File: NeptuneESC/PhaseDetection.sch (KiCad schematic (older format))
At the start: 9 parts

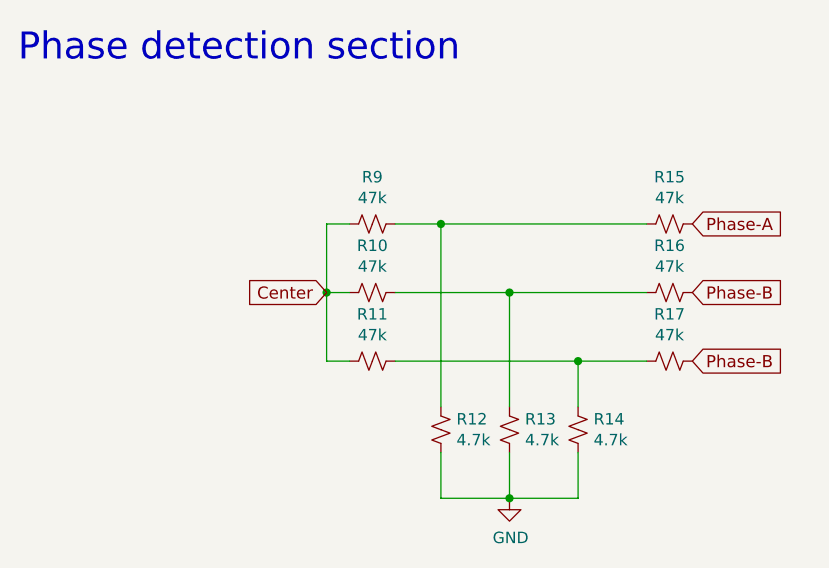
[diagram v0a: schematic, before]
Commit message: Innitial layout
Need to add motor pads
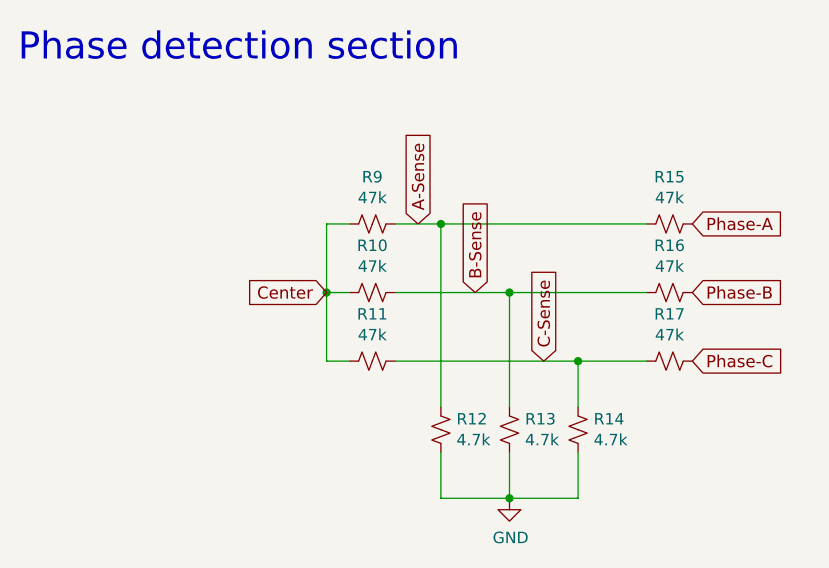
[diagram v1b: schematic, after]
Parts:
- R10, R11, R12, R13, R14, R15, R16, R17, R9: footprint (none) -> Resistor_SMD:R_0402_1005Metric
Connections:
- net Phase-B: no longer R17.1
- net A-Sense: now reaches R12.1, R15.2, R9.1
- net B-Sense: now reaches R10.1, R13.1, R16.2
- net C-Sense: now reaches R11.1, R14.1, R17.2
- new net Phase-C: R17.1
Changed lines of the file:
@@
 F 0 "R9" V 2895 2200 50  0000 C CNN
 F 1 "47k" V 2986 2200 50  0000 C CNN
-F 2 "" H 3100 2200 50  0001 C CNN
+F 2 "Resistor_SMD:R_0402_1005Metric" H 3100 2200 50  0001 C CNN
 F 3 "~" H 3100 2200 50  0001 C CNN
 F 4 "C25792" V 3100 2200 50  0001 C CNN "JLCPCB"
@@
 F 0 "R10" V 2895 2500 50  0000 C CNN
 F 1 "47k" V 2986 2500 50  0000 C CNN
-F 2 "" H 3100 2500 50  0001 C CNN
+F 2 "Resistor_SMD:R_0402_1005Metric" H 3100 2500 50  0001 C CNN
 F 3 "~" H 3100 2500 50  0001 C CNN
 F 4 "C25792" V 3100 2500 50  0001 C CNN "JLCPCB"
@@
 F 0 "R11" V 2895 2800 50  0000 C CNN
 F 1 "47k" V 2986 2800 50  0000 C CNN
-F 2 "" H 3100 2800 50  0001 C CNN
+F 2 "Resistor_SMD:R_0402_1005Metric" H 3100 2800 50  0001 C CNN
 F 3 "~" H 3100 2800 50  0001 C CNN
 F 4 "C25792" V 3100 2800 50  0001 C CNN "JLCPCB"
@@
 F 0 "R15" V 4195 2200 50  0000 C CNN
 F 1 "47k" V 4286 2200 50  0000 C CNN
-F 2 "" H 4400 2200 50  0001 C CNN
+F 2 "Resistor_SMD:R_0402_1005Metric" H 4400 2200 50  0001 C CNN
 F 3 "~" H 4400 2200 50  0001 C CNN
 F 4 "C25792" V 4400 2200 50  0001 C CNN "JLCPCB"
@@
 F 0 "R16" V 4195 2500 50  0000 C CNN
 F 1 "47k" V 4286 2500 50  0000 C CNN
-F 2 "" H 4400 2500 50  0001 C CNN
+F 2 "Resistor_SMD:R_0402_1005Metric" H 4400 2500 50  0001 C CNN
 F 3 "~" H 4400 2500 50  0001 C CNN
 F 4 "C25792" V 4400 2500 50  0001 C CNN "JLCPCB"
@@
 F 0 "R17" V 4195 2800 50  0000 C CNN
 F 1 "47k" V 4286 2800 50  0000 C CNN
-F 2 "" H 4400 2800 50  0001 C CNN
+F 2 "Resistor_SMD:R_0402_1005Metric" H 4400 2800 50  0001 C CNN
 F 3 "~" H 4400 2800 50  0001 C CNN
 F 4 "C25792" V 4400 2800 50  0001 C CNN "JLCPCB"
@@
 Phase-B
 Text GLabel 4500 2800 2    53   Input ~ 0
-Phase-B
+Phase-C
 Wire Wire Line
 	3200 2800 4000 2800
@@
 F 0 "R12" H 3468 3146 50  0000 L CNN
 F 1 "4.7k" H 3468 3055 50  0000 L CNN
-F 2 "" H 3400 3100 50  0001 C CNN
+F 2 "Resistor_SMD:R_0402_1005Metric" H 3400 3100 50  0001 C CNN
 F 3 "~" H 3400 3100 50  0001 C CNN
 F 4 "C25900" H 3400 3100 50  0001 C CNN "JLCPCB"
@@
 F 0 "R13" H 3768 3146 50  0000 L CNN
 F 1 "4.7k" H 3768 3055 50  0000 L CNN
-F 2 "" H 3700 3100 50  0001 C CNN
+F 2 "Resistor_SMD:R_0402_1005Metric" H 3700 3100 50  0001 C CNN
 F 3 "~" H 3700 3100 50  0001 C CNN
 F 4 "C25900" H 3700 3100 50  0001 C CNN "JLCPCB"
@@
 F 0 "R14" H 4068 3146 50  0000 L CNN
 F 1 "4.7k" H 4068 3055 50  0000 L CNN
-F 2 "" H 4000 3100 50  0001 C CNN
+F 2 "Resistor_SMD:R_0402_1005Metric" H 4000 3100 50  0001 C CNN
 F 3 "~" H 4000 3100 50  0001 C CNN
 F 4 "C25900" H 4000 3100 50  0001 C CNN "JLCPCB"
@@
 Text Notes 1550 1500 0    118  ~ 0
 Phase detection section
+Text GLabel 3300 2200 1    53   Input ~ 0
+A-Sense
+Text GLabel 3550 2500 1    53   Input ~ 0
+B-Sense
+Text GLabel 3850 2800 1    53   Input ~ 0
+C-Sense
 $EndSCHEMATC
